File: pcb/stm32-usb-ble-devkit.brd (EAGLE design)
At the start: 90 x 50 mm, 102 parts, among them CN1 USB-MICROB-2TABS, CN2 USB-C-2.0-FEMALE, CN3 USB-C-2.0-FEMALE, Q2 AO3402, Q4 AO3401, U1 STM32F103-48LQFP, U2 STM32F205-64, U3 TUSB320, U4 TUSB320, U5 HOLYIOT-17051-NRF51822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

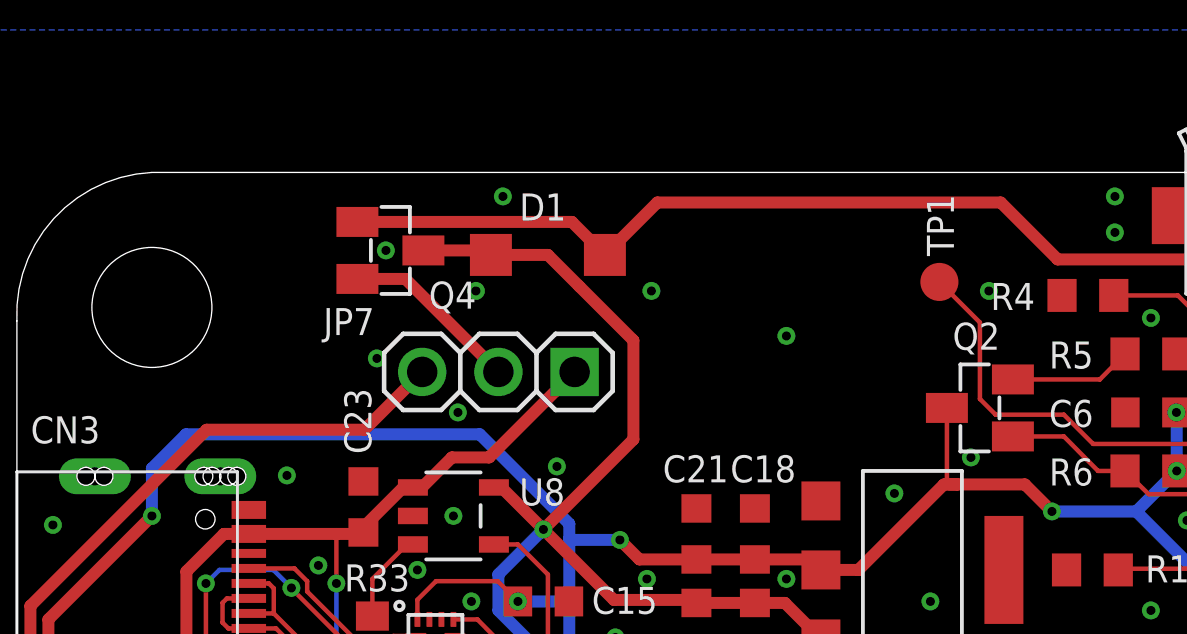
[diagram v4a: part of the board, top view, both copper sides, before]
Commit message: pcb: Add header exposing supply voltages
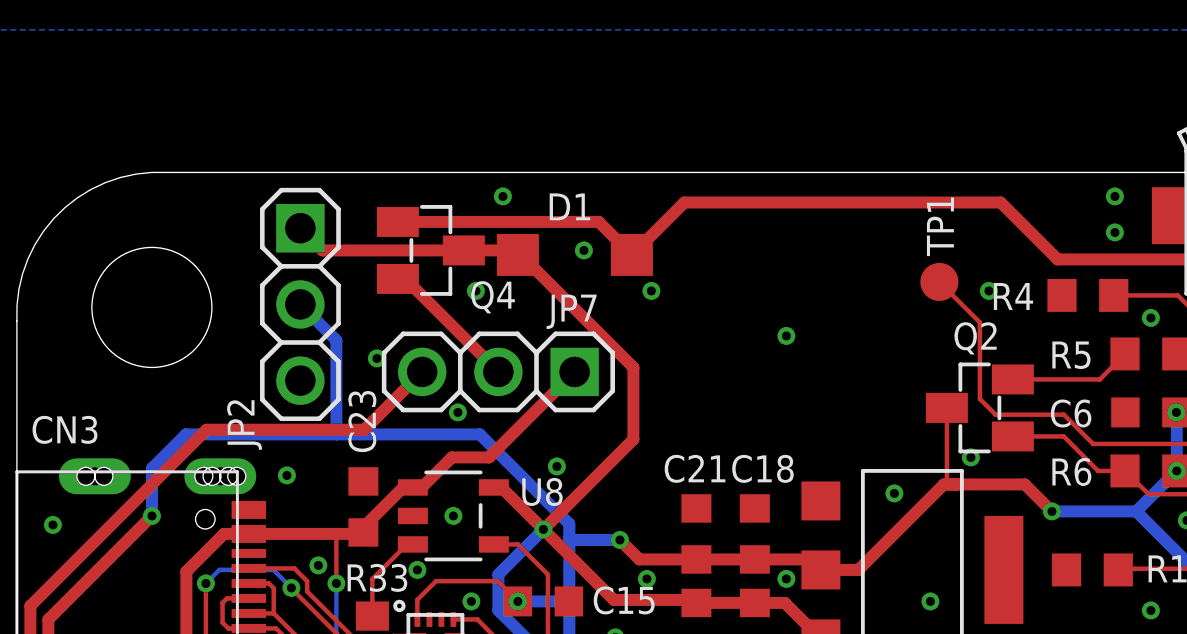
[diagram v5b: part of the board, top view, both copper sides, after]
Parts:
- added JP2: (no value), tuetuopay:1X03
- moved Q4 1.35 mm to (13.8, 47.4)
- moved D1 0.90 mm to (18.6, 47.2)
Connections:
- net +3V3: now also JP2.2
- net +5V: now also JP2.1
- net GND: now also JP2.3
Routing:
- net +3V3: track 267.0 -> 271.8 mm
- net +5V: track 60.5 -> 64.3 mm
- net STLINK_USB_VBUS: track 43.9 -> 42.5 mm
- net USB_FS_HS_VBUS: track 5.98 -> 4.63 mm
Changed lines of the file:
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@@
 </element>
 <element name="JP7" library="tuetuopay" package="1X03" package3d_urn="urn:adsk.eagle:package:22458/2" value="" x="16.05" y="43.35" smashed="yes" rot="R180">
-<attribute name="NAME" x="10.2138" y="44.5788" size="0.9" layer="25" ratio="10"/>
+<attribute name="NAME" x="17.7138" y="45.0288" size="0.9" layer="25" ratio="10"/>
 <attribute name="VALUE" x="19.86" y="46.525" size="1.27" layer="27" rot="R180"/>
 </element>
@@
 <attribute name="VALUE" x="39.637" y="14.07" size="1.27" layer="27" ratio="10" rot="R90"/>
 </element>
-<element name="Q4" library="tuetuopay" package="SOT23-3" value="AO3401" x="12.45" y="47.4" smashed="yes" rot="R270">
-<attribute name="NAME" x="13.73" y="46.36" size="0.9" layer="21" align="top-left"/>
+<element name="Q4" library="tuetuopay" package="SOT23-3" value="AO3401" x="13.8" y="47.4" smashed="yes" rot="R270">
+<attribute name="NAME" x="15.08" y="46.36" size="0.9" layer="21" align="top-left"/>
 </element>
 <element name="R1" library="tuetuopay" package="R0603" value="100k" x="35.85" y="36.75" smashed="yes" rot="R180">
@@
 <attribute name="VALUE" x="61.245" y="21.635" size="1.27" layer="27" rot="R270"/>
 </element>
-<element name="D1" library="tuetuopay" package="SOD123" value="MBR0540T1" x="17.7" y="47.25" smashed="yes">
-<attribute name="NAME" x="16.75" y="48.4" size="0.9" layer="25"/>
-<attribute name="VALUE" x="16.6" y="44.95" size="1.27" layer="27"/>
+<element name="D1" library="tuetuopay" package="SOD123" value="MBR0540T1" x="18.6" y="47.25" smashed="yes">
+<attribute name="NAME" x="17.65" y="48.4" size="0.9" layer="25"/>
+<attribute name="VALUE" x="17.5" y="44.95" size="1.27" layer="27"/>
 </element>
 <element name="U7" library="tuetuopay" package="SOT23-5" value="SY6280" x="15.6" y="11.4" smashed="yes" rot="R270">
@@
 </element>
 <element name="C23" library="tuetuopay" package="0603" value="10u" x="11.55" y="38.85" smashed="yes" rot="R90">
-<attribute name="NAME" x="11.815" y="40.615" size="0.9" layer="25" rot="R90"/>
+<attribute name="NAME" x="11.965" y="40.615" size="0.9" layer="25" rot="R90"/>
 <attribute name="VALUE" x="13.455" y="38.215" size="1.27" layer="27" rot="R90"/>
 </element>
@@
 <attribute name="NAME" x="79.4438" y="4.3788" size="0.9" layer="25" ratio="10"/>
 <attribute name="VALUE" x="68.72" y="1.625" size="1.27" layer="27"/>
+</element>
+<element name="JP2" library="tuetuopay" package="1X03" package3d_urn="urn:adsk.eagle:package:22458/2" value="" x="9.45" y="45.6" smashed="yes" rot="R270">
+<attribute name="NAME" x="7.9212" y="40.8138" size="0.9" layer="25" ratio="10" rot="R90"/>
+<attribute name="VALUE" x="6.275" y="49.41" size="1.27" layer="27" rot="R270"/>
 </element>
 </elements>
@@
 <wire x1="4.5" y1="38.55" x2="4.5" y2="40.13350625" width="0.4" layer="16"/>
 <wire x1="4.5" y1="40.13350625" x2="5.63649375" y2="41.27" width="0.4" layer="16"/>
-<wire x1="15.43" y1="41.27" x2="5.63649375" y2="41.27" width="0.4" layer="16"/>
+<wire x1="15.43" y1="41.27" x2="10.65" y2="41.27" width="0.4" layer="16"/>
 <contactref element="C18" pad="1"/>
 <contactref element="U6" pad="2"/>
 <contactref element="C21" pad="1"/>
 <via x="20.1" y="37.75" extent="1-16" drill="0.3"/>
+<wire x1="10.65" y1="41.27" x2="5.63649375" y2="41.27" width="0.4" layer="16"/>
 <wire x1="26.8" y1="36.75" x2="28.05" y2="36.75" width="0.4" layer="1"/>
 <wire x1="26.35" y1="26.43" x2="26.35" y2="25.3893375" width="0.3" layer="1"/>
@@
 <wire x1="63.6" y1="35" x2="63.6" y2="25.95" width="0.15" layer="1"/>
 <wire x1="61.2" y1="21.8625" x2="59.25" y2="21.8625" width="0.15" layer="1"/>
+<contactref element="JP2" pad="2"/>
+<wire x1="9.45" y1="45.6" x2="10.65" y2="44.4" width="0.4" layer="16"/>
+<wire x1="10.65" y1="44.4" x2="10.65" y2="41.27" width="0.4" layer="16"/>
 </signal>
 <signal name="GND">
@@
 <via x="1.2" y="38.25" extent="1-16" drill="0.3"/>
 <via x="12" y="43.8" extent="1-16" drill="0.3"/>
-<via x="12.3" y="47.4" extent="1-16" drill="0.3"/>
+<via x="18.9" y="47.4" extent="1-16" drill="0.3"/>
 <via x="16.2" y="49.2" extent="1-16" drill="0.3"/>
 <via x="18" y="40.2" extent="1-16" drill="0.3"/>
@@
 <contactref element="JP1" pad="4"/>
 <via x="70.95" y="7.95" extent="1-16" drill="0.3"/>
+<contactref element="JP2" pad="3"/>
 </signal>
 <signal name="STLINK_PC13">
@@
 <wire x1="43.65" y1="47.1" x2="34.693" y2="47.1" width="0.4" layer="1"/>
 <contactref element="D1" pad="A"/>
-<wire x1="11.35" y1="48.35" x2="18.5" y2="48.35" width="0.4" layer="1"/>
-<wire x1="18.5" y1="48.35" x2="19.6" y2="47.25" width="0.4" layer="1"/>
-<wire x1="19.6" y1="47.25" x2="21.348" y2="48.998" width="0.4" layer="1"/>
-<wire x1="21.348" y1="48.998" x2="32.795" y2="48.998" width="0.4" layer="1"/>
+<wire x1="12.7" y1="48.35" x2="19.4" y2="48.35" width="0.4" layer="1"/>
+<wire x1="19.4" y1="48.35" x2="20.5" y2="47.25" width="0.4" layer="1"/>
+<wire x1="20.5" y1="47.25" x2="22.248" y2="48.998" width="0.4" layer="1"/>
+<wire x1="22.248" y1="48.998" x2="32.795" y2="48.998" width="0.4" layer="1"/>
 </signal>
 <signal name="STM_OSC_IN">
@@
 <wire x1="17.55" y1="38.1" x2="19.9" y2="35.75" width="0.4" layer="1"/>
 <contactref element="D1" pad="C"/>
-<wire x1="13.55" y1="47.4" x2="15.65" y2="47.4" width="0.4" layer="1"/>
-<wire x1="15.65" y1="47.4" x2="15.8" y2="47.25" width="0.4" layer="1"/>
+<wire x1="14.9" y1="47.4" x2="16.55" y2="47.4" width="0.4" layer="1"/>
+<wire x1="16.55" y1="47.4" x2="16.7" y2="47.25" width="0.4" layer="1"/>
 <wire x1="19.9" y1="35.75" x2="22.55" y2="35.75" width="0.4" layer="1"/>
 <wire x1="22.55" y1="35.75" x2="22.65" y2="35.65" width="0.4" layer="1"/>
@@
 <wire x1="24.6" y1="35.65" x2="25.6" y2="35.65" width="0.4" layer="1"/>
 <wire x1="25.6" y1="35.65" x2="26.8" y2="34.45" width="0.4" layer="1"/>
-<wire x1="15.8" y1="47.25" x2="17.7" y2="47.25" width="0.4" layer="1"/>
-<wire x1="18.75" y1="46.2" x2="20.55" y2="44.4" width="0.4" layer="1"/>
+<wire x1="16.7" y1="47.25" x2="16.8" y2="47.25" width="0.4" layer="1"/>
+<wire x1="18.45" y1="45.6" x2="20.55" y2="43.5" width="0.4" layer="1"/>
 <wire x1="20.55" y1="41.1" x2="17.55" y2="38.1" width="0.4" layer="1"/>
-<wire x1="17.7" y1="47.25" x2="18.75" y2="46.2" width="0.4" layer="1"/>
-<wire x1="20.55" y1="44.4" x2="20.55" y2="41.1" width="0.4" layer="1"/>
+<wire x1="16.8" y1="47.25" x2="18.45" y2="45.6" width="0.4" layer="1"/>
+<wire x1="20.55" y1="43.5" x2="20.55" y2="41.1" width="0.4" layer="1"/>
 <contactref element="U7" pad="5"/>
 <contactref element="U8" pad="5"/>
@@
 <wire x1="16.05" y1="35.4" x2="16.05" y2="36.6" width="0.4" layer="16"/>
 <wire x1="16.05" y1="36.6" x2="17.55" y2="38.1" width="0.4" layer="16"/>
+<contactref element="JP2" pad="1"/>
+<wire x1="14.9" y1="47.4" x2="10.19" y2="47.4" width="0.4" layer="1"/>
+<wire x1="10.19" y1="47.4" x2="9.45" y2="48.14" width="0.4" layer="1"/>
 </signal>
 <signal name="STM_DBG_PIN2">
@@
 <contactref element="Q4" pad="2"/>
 <contactref element="JP7" pad="2"/>
-<wire x1="11.35" y1="46.45" x2="12.95" y2="46.45" width="0.4" layer="1"/>
+<wire x1="12.7" y1="46.45" x2="12.95" y2="46.45" width="0.4" layer="1"/>
 <wire x1="12.95" y1="46.45" x2="16.05" y2="43.35" width="0.4" layer="1"/>
 </signal>
